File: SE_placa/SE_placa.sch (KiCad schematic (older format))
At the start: 17 parts, among them J1 3.3 V, J2 Micro_SD_Card, U1 ESP32-WROVER, U2 RFM95W-915S2

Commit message: Organizar
Se organizo la distribución de los espacios, se separo la fuente del ESP32 y la fuente de alimentación
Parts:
- removed C?: 1uF, symbol Device:C
- added C?: C, symbol Device:C
- added L?: L, symbol Device:L
- C1: renamed from C?; footprint (none) -> Capacitor_SMD:C_0805_2012Metric
- J1: value 3.3 V -> Bateria 3.3V
- gave numbers to parts that had none: 11
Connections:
- net labels added: EN-ESP, VCC-ESP, VCCESP
- wire segments 93 -> 96
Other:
- note added: "DISTRIBUCION I/O"
- note added: "FUENTE/ALIMENTACIÓN:"
- note added: "I2C:"
- note added: "MICRO SD:\n"
- note added: "MODULO LORA"
- note added: "MODULO-ESP32\n"
- note added: "UART:"
- note removed: "Placa SE 2021"
- moved on the sheet: C1, J1, J2, J3, J5, J6, J7, R1, R2, R3, R4, R5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

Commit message: Cambio modelo de Hoja A3
organizo hoja de esquematico a formato A3. Incluyo libreria de conector UFL. Organizo Alimentacion, incluyo bobinas para I/O salidas. Incluyo switches de EN y de Programacion IO0, IO2, incluyo algunos condensadores y leds
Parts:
- removed J3: Boot Option, symbol Connector_Generic:Conn_01x02
- removed J4: Conn_01x08, symbol Connector_Generic:Conn_01x08
- added C? (x3): 0.1uF/16V(10%), symbol Device:C
- added C?: C, symbol Device:C
- added C?: 100uF/16V(10%), symbol Device:C
- added C?: 1uF/16V(10%), symbol Device:C
- added D? (x6): LED, symbol Device:LED
- added J?: Conn_02x06_Top_Bottom, symbol Connector_Generic:Conn_02x06_Top_Bottom
- added J?: U.FL-R-SMT(01), HRS_U.FL-R-SMT(01), symbol U.FL-R-SMT_01_:U.FL-R-SMT(01)
- added L? (x7): L, symbol Device:L
- added Q? (x2): BSS138, Package_TO_SOT_SMD:SOT-23, symbol Transistor_FET:BSS138
- added R? (x2): 10K(1%), symbol Device:R
- added R? (x2): 1K(1%), symbol Device:R
- added R? (x6): 2K, symbol Device:R
- added SW?: SW_Push_ESP_RST, symbol Switch:SW_Push
- added SW?: SW_Push, symbol Switch:SW_Push
- C?: value C -> 1uF/16V(10%)
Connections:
- net labels added: ESP-EN, I035-I35, IO0, IO2, IO34-I34, IO35-I35, IO36-I36, IO39-I39, VCC-LORA
- net labels removed: VCCESP
- wire segments 96 -> 190
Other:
- note added: "DOWNLOAD BUTTON\n"
- note added: "ENABLE/RESET\n\n"
- note added: "LEDS"
- note added: "MICRO SD(SPI2)\n"
- note added: "MODULO LORA\n(SPI1)\n"
- note added: "POWER"
- note removed: "DISTRIBUCION I/O"
- note removed: "FUENTE/ALIMENTACIÓN:"
- note removed: "MICRO SD:\n"
- note removed: "MODULO LORA"
- moved on the sheet: C1, C?, J1, J2, J5, J6, J7, L?, R1, R2, R3, R4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

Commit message: Finalizacion del layout
Se ordeno nuevamente el layout, se completaron conexion de los modulos, se incluyo conexion de I/O del modulo lora al ESP, se incluyeron los I/O de lora.  se amplio la cantidad de pines del conector de IO del ESP32. Se incluyeron valores de bobinas de ferrita para los lazos de alimentacion. Se modifico el excel con Pin out y se incluyo una hoja con pines de lora.
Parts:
- removed J7: I2C-1, symbol Connector_Generic:Conn_01x04
- removed J?: Conn_02x06_Top_Bottom, symbol Connector_Generic:Conn_02x06_Top_Bottom
- removed L? (x6): L, symbol Device:L
- added J?: I2C-1, symbol Connector_Generic:Conn_01x04
- added J?: Conn_02x03_LORA_IO, symbol Connector_Generic:Conn_02x03_Top_Bottom
- added J?: Conn_02x07_ESP32_IO, symbol Connector_Generic:Conn_02x07_Top_Bottom
- added L? (x2): 2A 120 ohm, symbol Device:L
- added R? (x10): 0R(1%), symbol Device:R
- C?: value 1uF/16V(10%) -> 0.1uF/16V(10%)
- L? (x2): value L -> 2A 120 ohm
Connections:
- net labels added: IO12, IO25, IO32, IO33, L-DIO1, L-DIO2
- net labels removed: VCC
- wire segments 190 -> 228
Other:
- note added: "ESP32-IO\n"
- note added: "I2C- BMP180 - BY-68"
- note added: "I2C-spare"
- note added: "I2C\n"
- note added: "LORA-IO\n"
- note removed: "I2C:"
- moved on the sheet: C?, J5, J6

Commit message: Se asociaron footprints
Se pusieron los footprints y se pudo asociar las librerias de los elementos, escogiendolos comercialmente y midiendo con los que ya tengo en mi poder.
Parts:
- C1: footprint Capacitor_SMD:C_0805_2012Metric -> Capacitor_SMD:C_0805_2012Metric_Pad1.18x1.45mm_HandSolder
- C2, C3, C4, C6, C7, C8: renamed from C?; footprint (none) -> Capacitor_SMD:C_0805_2012Metric_Pad1.18x1.45mm_HandSolder
- C5: renamed from C?; value C -> 0.1uF; footprint (none) -> Capacitor_SMD:C_0805_2012Metric_Pad1.18x1.45mm_HandSolder
- D1, D2, D3, D4, D5, D6: renamed from D?; footprint (none) -> LED_SMD:LED_0805_2012Metric_Pad1.15x1.40mm_HandSolder
- J1: footprint (none) -> Connector_PinHeader_2.54mm:PinHeader_1x02_P2.54mm_Vertical
- J2: footprint (none) -> Connector_Card:microSD_HC_Molex_104031-0811
- J3: renamed from J?; footprint (none) -> Connector_PinSocket_2.54mm:PinSocket_2x07_P2.54mm_Vertical
- J4: renamed from J?; footprint (none) -> Connector_PinSocket_2.54mm:PinSocket_2x03_P2.54mm_Vertical
- J5: footprint (none) -> Connector_PinSocket_2.54mm:PinSocket_1x04_P2.54mm_Vertical
- J6: renamed from J?; footprint HRS_U.FL-R-SMT(01) -> Connector_Coaxial:U.FL_Molex_MCRF_73412-0110_Vertical
- J7: renamed from J6; footprint (none) -> Connector_PinSocket_2.54mm:PinSocket_1x04_P2.54mm_Vertical
- J8: renamed from J?; footprint (none) -> Connector_PinSocket_2.54mm:PinSocket_1x04_P2.54mm_Vertical
- L1, L2, L3, L4: renamed from L?; footprint (none) -> Inductor_SMD:L_0805_2012Metric_Pad1.15x1.40mm_HandSolder
- R1, R2: footprint (none) -> Resistor_SMD:R_0805_2012Metric_Pad1.20x1.40mm_HandSolder
- R10, R11, R12, R13, R14, R15, R16, R17, R18, R19, R20, R21, R22, R23, R24, R25, R26, R3, R6, R7: renamed from R?; footprint (none) -> Resistor_SMD:R_0805_2012Metric_Pad1.20x1.40mm_HandSolder
- R4: renamed from R3; footprint (none) -> Resistor_SMD:R_0805_2012Metric_Pad1.20x1.40mm_HandSolder
- R5: renamed from R4; footprint (none) -> Resistor_SMD:R_0805_2012Metric_Pad1.20x1.40mm_HandSolder
- R8: renamed from R5; footprint (none) -> Resistor_SMD:R_0805_2012Metric_Pad1.20x1.40mm_HandSolder
- R9: renamed from R6; footprint (none) -> Resistor_SMD:R_0805_2012Metric_Pad1.20x1.40mm_HandSolder
- SW1: renamed from SW?; value SW_Push -> SW_Push_Download; footprint (none) -> B3U-1000P:SW_B3U-1000P
- SW2: renamed from SW?; footprint (none) -> B3U-1000P:SW_B3U-1000P
- U1: footprint (none) -> ESP32-WROVER-I:XCVR_ESP32-WROVER-I
- U2: footprint (none) -> RF_Module:HOPERF_RFM9XW_SMD
- gave numbers to parts that had none: 2

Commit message: Actualizacion de huellas y correccion de  errores de layout
Corrigieron los errores de layout, se incluyeron power conector y se señalaron los pines que no se concetan,  se actualizaron huellas a elementos comerciales, se cambio la huella del Micro SD y del conector de antena del modulo lora. Se inicio con el diseño del PCB  haciendo una primera distribucion de los elementos
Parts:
- removed J2: Micro_SD_Card, Connector_Card:microSD_HC_Molex_104031-0811, symbol Connector:Micro_SD_Card
- added J9: Micro_SD_Card_Det_Hirose_DM3AT, Connector_Card:microSD_HC_Hirose_DM3AT-SF-PEJM5, symbol Connector:Micro_SD_Card_Det_Hirose_DM3AT
- J6: footprint Connector_Coaxial:U.FL_Molex_MCRF_73412-0110_Vertical -> U:HRS_U.FL-R-SMT(01)
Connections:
- net labels removed: I035-I35
- wire segments 228 -> 239
- no-connect marks 0 -> 11
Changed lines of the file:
@@
-$EndComp
-$Comp
-L Connector:Micro_SD_Card J2
-U 1 1 6077F42C
-P 5085 9700
-F 0 "J2" H 5035 10417 50  0000 C CNN
-F 1 "Micro_SD_Card" H 5035 10326 50  0000 C CNN
-F 2 "Connector_Card:microSD_HC_Molex_104031-0811" H 6235 10000 50  0001 C CNN
-F 3 "http://katalog.we-online.de/em/datasheet/693072010801.pdf" H 5085 9700 50  0001 C CNN
-	1    5085 9700
-	1    0    0    -1
 $EndComp
 $Comp
@@
 	13410 3510 13610 3510
 Wire Wire Line
-	13310 2310 13310 2010
+	13310 2310 13310 2060
 Wire Wire Line
 	11060 2610 12810 2610
@@
 Text Label 11060 3710 0    50   ~ 0
 SPI1-RST
-Wire Wire Line
-	9310 2410 9010 2410
 Text Label 9010 2410 0    50   ~ 0
 GND
@@
 Connection ~ 4035 9400
 Wire Wire Line
-	4035 9400 4185 9400
-Wire Wire Line
 	3785 9300 3785 9500
 Connection ~ 3785 9500
 Wire Wire Line
-	3785 9500 4185 9500
-Wire Wire Line
 	3535 9300 3535 9600
 Connection ~ 3535 9600
 Wire Wire Line
-	3535 9600 4185 9600
-Wire Wire Line
 	3285 9300 3285 9800
 Connection ~ 3285 9800
 Wire Wire Line
-	3285 9800 4185 9800
-Wire Wire Line
 	3035 9300 3035 10000
 Connection ~ 3035 10000
 Wire Wire Line
-	3035 10000 4185 10000
-Wire Wire Line
 	2785 9300 2785 10100
 Connection ~ 2785 10100
-Wire Wire Line
-	2785 10100 4185 10100
 Wire Wire Line
 	4035 9000 4035 8800
@@
 Connection ~ 2485 9900
 Wire Wire Line
-	2485 9900 4185 9900
-Wire Wire Line
 	2485 9000 2485 8800
 Wire Wire Line
@@
 Wire Wire Line
 	2285 8800 2485 8800
-Wire Wire Line
-	2285 9700 4185 9700
 Connection ~ 2485 8800
 $Comp
@@
 Text Label 14435 6100 0    50   ~ 0
 VCC-ESP
-Wire Wire Line
-	9015 2510 9310 2510
 Text Notes 750  910  0    157  ~ 31
 POWER
@@
 Text Notes 12440 1130 0    157  ~ 31
 MODULO LORA\n(SPI1)\n
-Wire Wire Line
-	9310 2610 9015 2610
 Text Label 9015 2610 0    50   ~ 0
 EN-ESP
@@
 IO34-I34
 Text Label 8215 7265 0    50   ~ 0
-I035-I35
+IO35-I35
 Wire Wire Line
 	8620 2710 9310 2710
@@
 Text Label 7800 3010 0    50   ~ 0
 IO35-I35
-Wire Wire Line
-	7800 3010 8320 3010
 Wire Wire Line
 	8610 6765 8225 6765
@@
 $EndComp
 Wire Wire Line
-	2070 1510 2070 1710
+	2070 1510 2070 1555
 Connection ~ 2070 1710
 Wire Wire Line
@@
 F 0 "J6" H 14967 2650 50  0000 L CNN
 F 1 "U.FL-R-SMT(01)" H 15010 2535 50  0000 L CNN
-F 2 "Connector_Coaxial:U.FL_Molex_MCRF_73412-0110_Vertical" H 14765 2610 50  0001 L BNN
-F 3 "" H 14765 2610 50  0001 L BNN
+F 2 "U:HRS_U.FL-R-SMT(01)" H 14765 2610 50  0001 L BNN
+F 3 "https://www.sigmaelectronica.net/producto/con-u-fl-smd-m/" H 14765 2610 50  0001 L BNN
 F 4 "Hirose" H 14765 2610 50  0001 L BNN "MF"
 F 5 "U.FL Series 6 Ghz 50 Ohm Ultra-small SMT Coaxial Cable Receptacle" H 14765 2610 50  0001 L BNN "DESCRIPTION"
@@
 	1    0    0    -1
 $EndComp
+$Comp
+L power:PWR_FLAG #FLG0101
+U 1 1 60974DFB
+P 9005 2240
+F 0 "#FLG0101" H 9005 2315 50  0001 C CNN
+F 1 "PWR_FLAG" H 9005 2413 50  0000 C CNN
+F 2 "" H 9005 2240 50  0001 C CNN
+F 3 "~" H 9005 2240 50  0001 C CNN
+	1    9005 2240
+	1    0    0    -1
+$EndComp
+Wire Wire Line
+	9005 2240 9005 2410
+Wire Wire Line
+	9005 2410 9310 2410
+$Comp
+L power:PWR_FLAG #FLG0102
+U 1 1 6098BE32
+P 8735 2145
+F 0 "#FLG0102" H 8735 2220 50  0001 C CNN
+F 1 "PWR_FLAG" H 8735 2318 50  0000 C CNN
+F 2 "" H 8735 2145 50  0001 C CNN
+F 3 "~" H 8735 2145 50  0001 C CNN
+	1    8735 2145
+	1    0    0    -1
+$EndComp
+$Comp
+L power:PWR_FLAG #FLG0103
+U 1 1 6098C5D4
+P 8470 2070
+F 0 "#FLG0103" H 8470 2145 50  0001 C CNN
+F 1 "PWR_FLAG" H 8470 2243 50  0000 C CNN
+F 2 "" H 8470 2070 50  0001 C CNN
+F 3 "~" H 8470 2070 50  0001 C CNN
+	1    8470 2070
+	1    0    0    -1
+$EndComp
+Wire Wire Line
+	8735 2510 9310 2510
+Wire Wire Line
+	8470 2070 8470 2610
+Wire Wire Line
+	8470 2610 9310 2610
+Wire Wire Line
+	8735 2145 8735 2510
+$Comp
+L power:PWR_FLAG #FLG0104
+U 1 1 609FFFB7
+P 1905 1380
+F 0 "#FLG0104" H 1905 1455 50  0001 C CNN
+F 1 "PWR_FLAG" H 1905 1553 50  0000 C CNN
+F 2 "" H 1905 1380 50  0001 C CNN
+F 3 "~" H 1905 1380 50  0001 C CNN
+	1    1905 1380
+	1    0    0    -1
+$EndComp
+Wire Wire Line
+	1905 1555 2070 1555
+Connection ~ 2070 1555
+Wire Wire Line
+	2070 1555 2070 1710
+Wire Wire Line
+	1905 1555 1905 1380
+$Comp
+L power:PWR_FLAG #FLG0105
+U 1 1 60A40AD1
+P 13605 1970
+F 0 "#FLG0105" H 13605 2045 50  0001 C CNN
+F 1 "PWR_FLAG" H 13605 2143 50  0000 C CNN
+F 2 "" H 13605 1970 50  0001 C CNN
+F 3 "~" H 13605 1970 50  0001 C CNN
+	1    13605 1970
+	1    0    0    -1
+$EndComp
+Wire Wire Line
+	13605 1970 13605 2060
+Wire Wire Line
+	13605 2060 13310 2060
+Connection ~ 13310 2060
+Wire Wire Line
+	13310 2060 13310 2010
+NoConn ~ 11060 4110
+NoConn ~ 11060 4210
+NoConn ~ 11060 4310
+NoConn ~ 9310 4010
+NoConn ~ 9310 4110
+NoConn ~ 9310 4210
+NoConn ~ 13810 2710
+NoConn ~ 13810 2810
+NoConn ~ 13810 2910
+$Comp
+L power:PWR_FLAG #FLG0106
+U 1 1 60AED136
+P 2485 8595
+F 0 "#FLG0106" H 2485 8670 50  0001 C CNN
+F 1 "PWR_FLAG" H 2485 8768 50  0000 C CNN
+F 2 "" H 2485 8595 50  0001 C CNN
+F 3 "~" H 2485 8595 50  0001 C CNN
+	1    2485 8595
+	1    0    0    -1
+$EndComp
+Wire Wire Line
+	2485 8595 2485 8800
+Wire Wire Line
+	2485 8800 2485 8805
+Wire Wire Line
+	7800 3010 8320 3010
+Wire Wire Line
+	2785 10100 4185 10100
+Wire Wire Line
+	3035 10000 4185 10000
+Wire Wire Line
+	2485 9900 4185 9900
+Wire Wire Line
+	3285 9800 4185 9800
+Wire Wire Line
+	2285 9700 4185 9700
+Wire Wire Line
+	3535 9600 4185 9600
+Wire Wire Line
+	3785 9500 4185 9500
+Wire Wire Line
+	4035 9400 4185 9400
+$Comp
+L Connector:Micro_SD_Card_Det_Hirose_DM3AT J9
+U 1 1 60B99449
+P 5085 9800
+F 0 "J9" H 5035 10617 50  0000 C CNN
+F 1 "Micro_SD_Card_Det_Hirose_DM3AT" H 5035 10526 50  0000 C CNN
+F 2 "Connector_Card:microSD_HC_Hirose_DM3AT-SF-PEJM5" H 7135 10500 50  0001 C CNN
+F 3 "https://www.sigmaelectronica.net/producto/dm3at/" H 5085 9900 50  0001 C CNN
+	1    5085 9800
+	1    0    0    -1
+$EndComp
+NoConn ~ 4185 10200
+NoConn ~ 4185 10300
 $EndSCHEMATC

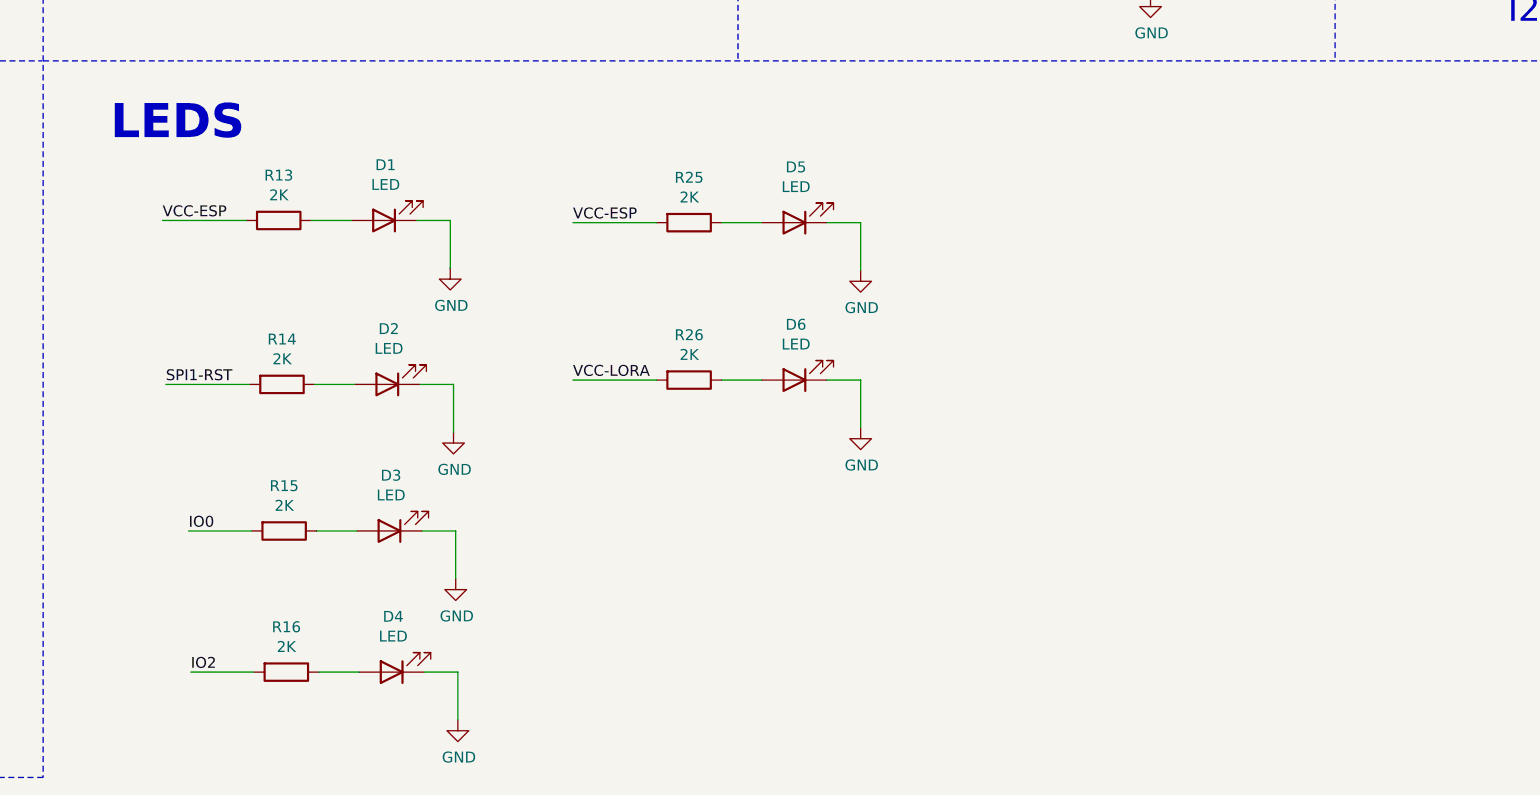
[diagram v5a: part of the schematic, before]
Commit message: Actualizacion de PCB solo rutas
Eliminado un led repetido, el led 5. Primer intento crudo de desarrollar la PCB sin estandares, tamaños de caminos u otras consideraciones tecnicas, solo ruteo para ir entendiendo y aprendiendo cual es la mejor ubicacion de los elementos, tambien saber si puedo llegar en algun momento a la meta de 52 mm X 40 mm.
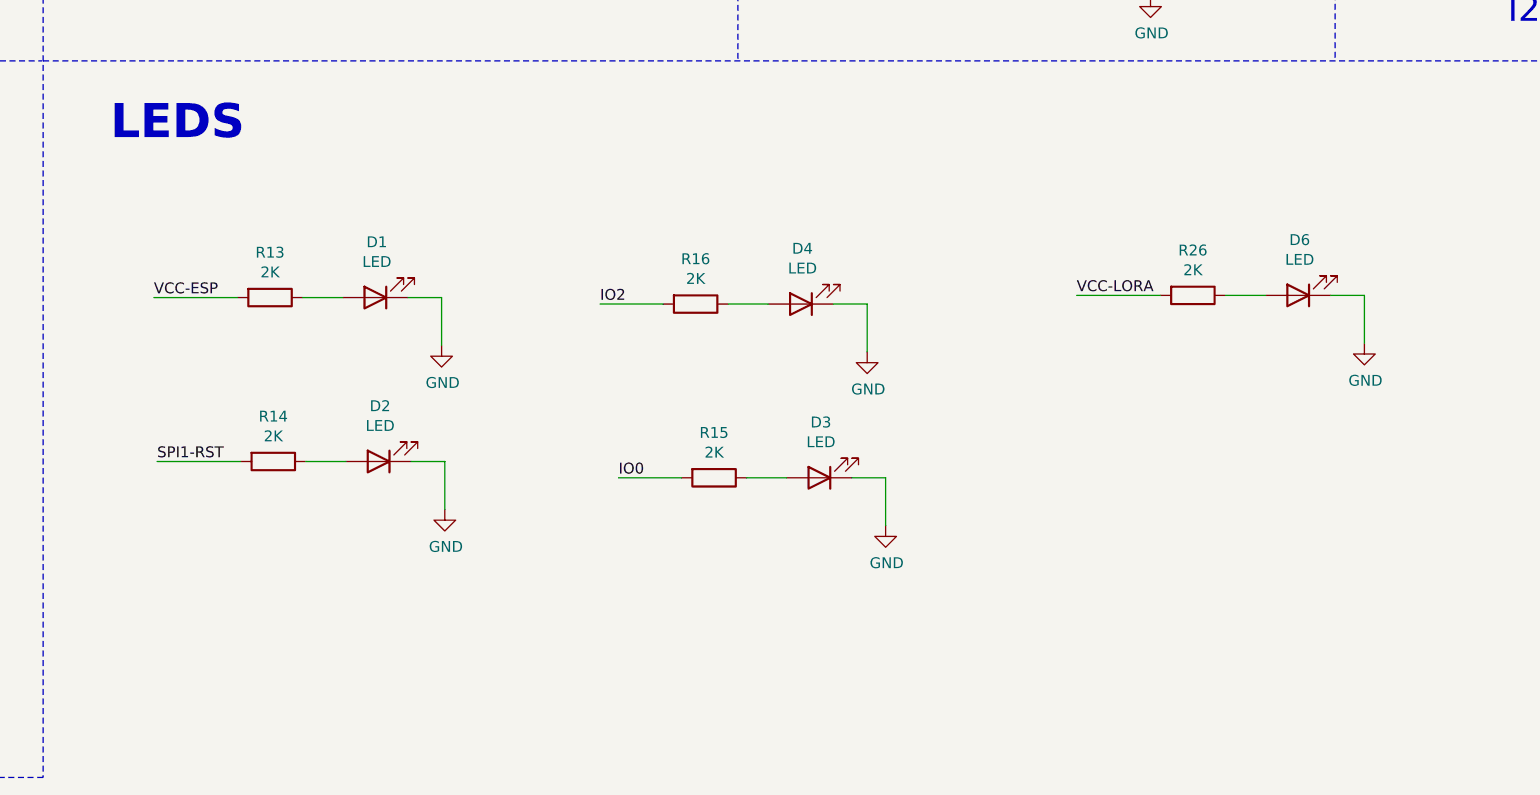
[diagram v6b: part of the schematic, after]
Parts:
- removed D5: LED, LED_SMD:LED_0805_2012Metric_Pad1.15x1.40mm_HandSolder, symbol Device:LED
- removed R25: 2K, Resistor_SMD:R_0805_2012Metric_Pad1.20x1.40mm_HandSolder, symbol Device:R
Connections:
- wire segments 239 -> 235
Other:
- moved on the sheet: D1, D2, D3, D4, D6, R13, R14, R15, R16, R26

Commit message: Corregida Grid, reinciado el PCB
Crroegido grid a 25 mil, reconectado el layout, se cambiaron ubicación de algunos elementos dentro de la sabana . se retiraron las resistencias de 0 ohm no necesarias en la I/O, se cambio bonina por resistencia de p ohm en diagrama reset se agregó resistencias pull up a I2C, , se reitaron resistencias pull up no necesarias en la conexion de la Micro SD. Se organizaron las fuentes de todo el circuito, 3.3V Alimentación 3V3 punto de conexion ESP  y 3.3VP punto de conexion Lora.
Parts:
- removed J8: I2C-1, Connector_PinSocket_2.54mm:PinSocket_1x04_P2.54mm_Vertical, symbol Connector_Generic:Conn_01x04
- removed L2: 2A 120 ohm, Inductor_SMD:L_0805_2012Metric_Pad1.15x1.40mm_HandSolder, symbol Device:L
- removed R1, R9: 10K, Resistor_SMD:R_0805_2012Metric_Pad1.20x1.40mm_HandSolder, symbol Device:R
- removed R17, R18, R19, R20, R21, R22, R23: 0R(1%), Resistor_SMD:R_0805_2012Metric_Pad1.20x1.40mm_HandSolder, symbol Device:R
- added J5: I2C-1, Connector_PinSocket_2.54mm:PinSocket_1x04_P2.54mm_Vertical, symbol Connector_Generic:Conn_01x04
- added R12, R13: 4.7K(5%), Resistor_SMD:R_0805_2012Metric_Pad1.20x1.40mm_HandSolder, symbol Device:R
- renumbered C5 to C4, C4 to C5, D2 to D1, D1 to D2, D6 to D5, J9 to J2, J7 to J4, J4 to J6, J6 to J7, J5 to J8, L3 to L2, L4 to L3, R2 to R1, R12 to R10, R10 to R11, R13 to R15, R15 to R17, R26 to R18, R3 to R2, R4 to R3, R5 to R4, R6 to R5, R7 to R6, R8 to R7, R24 to R8, R11 to R9
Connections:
- net labels added: +3.3VP, +3V3, I34, I35, I36, I39
- net labels removed: EN-ESP, IO34-I34, IO35-I35, IO36-I36, IO39-I39, VCC-ESP, VCC-LORA
- wire segments 235 -> 222
- no-connect marks 11 -> 13
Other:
- moved on the sheet: C1, C2, C3, C4, C6, C7, C8, D1, D2, D3, D4, D5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
